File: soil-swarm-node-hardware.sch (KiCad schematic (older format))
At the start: 21 parts, among them J3 Conn_01x07, U1 RFD77101, U4 DS18B20U, U5 SST26VF016B

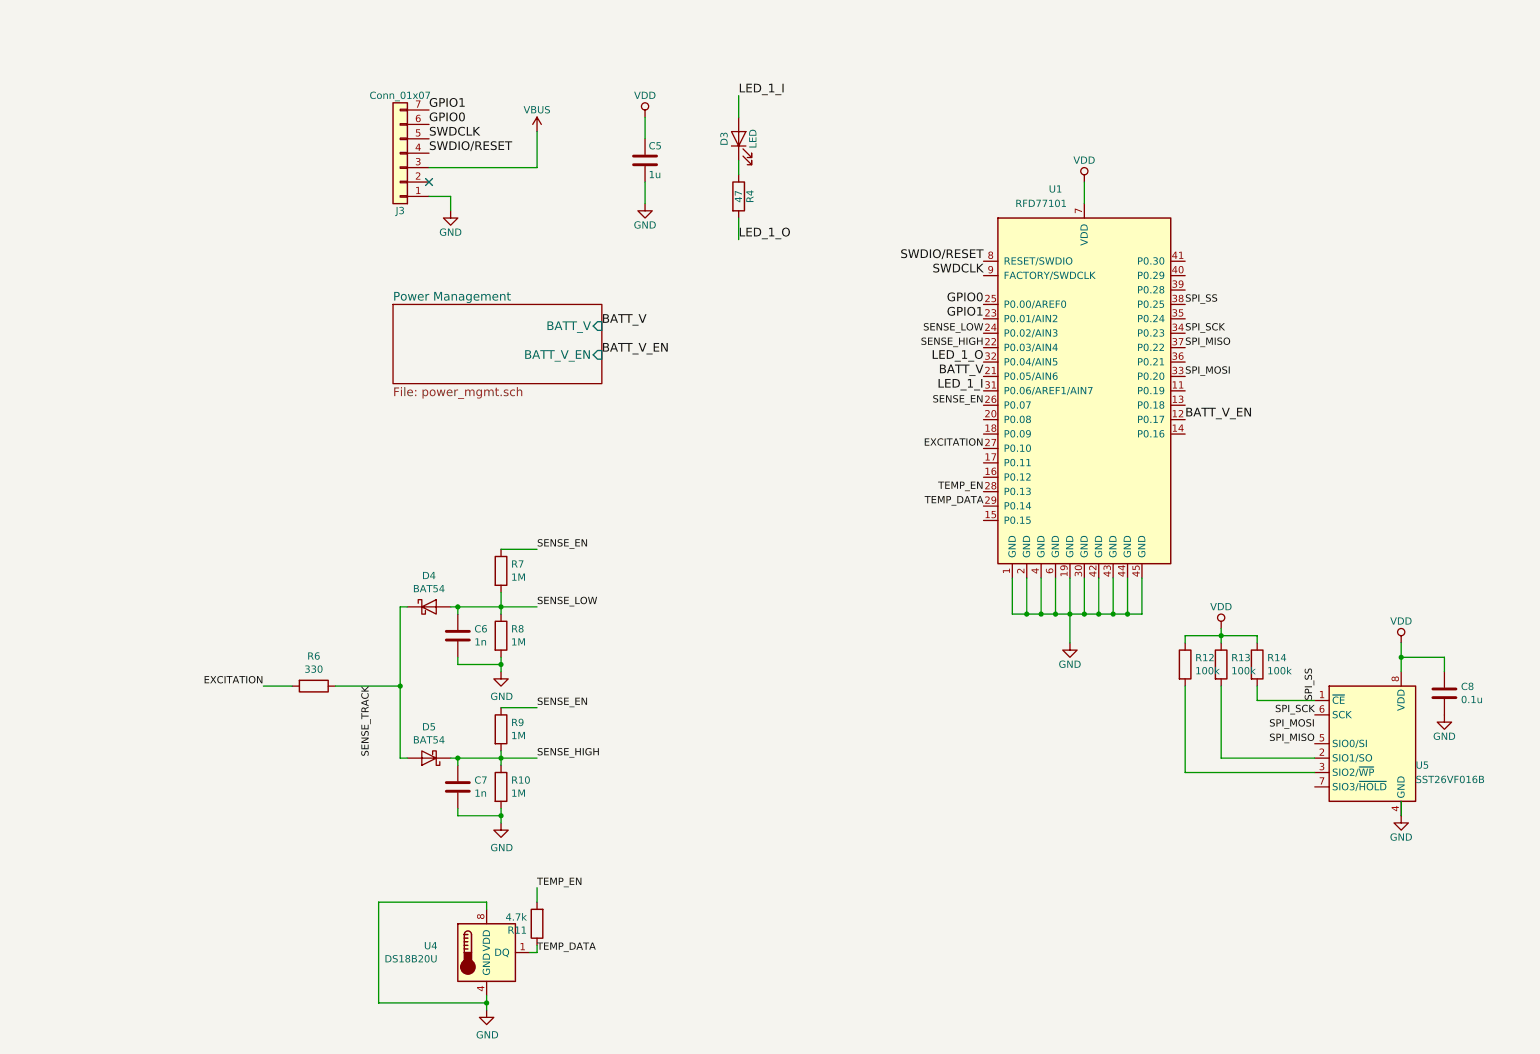
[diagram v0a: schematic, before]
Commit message: create new version based on nRF52840
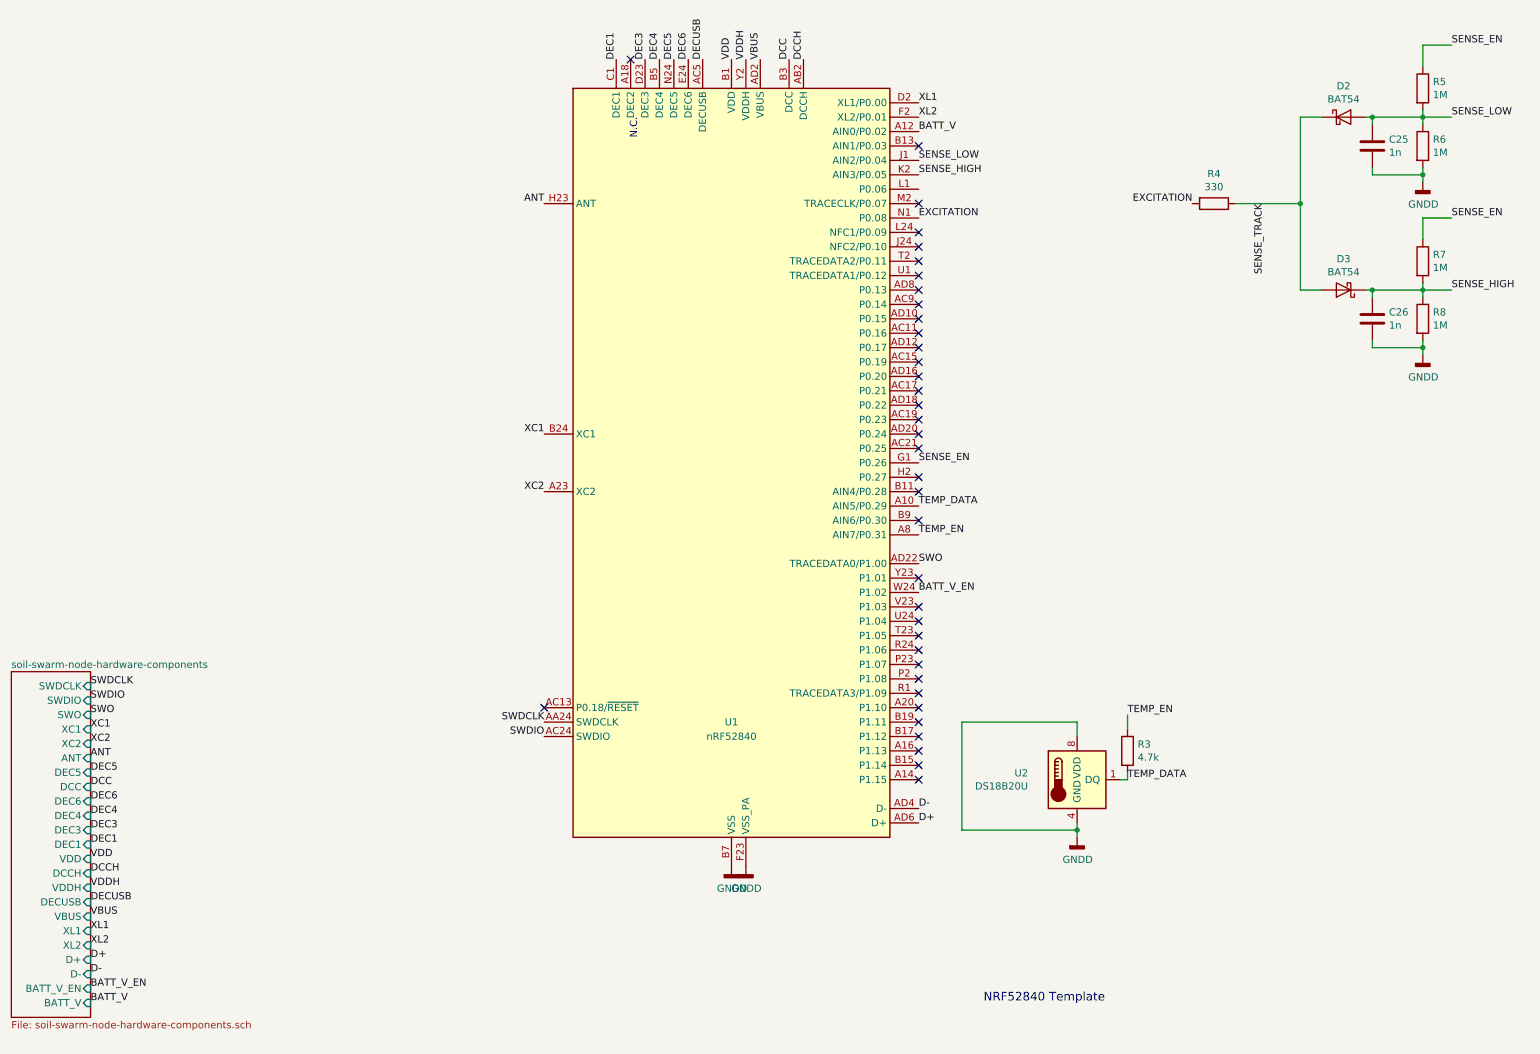
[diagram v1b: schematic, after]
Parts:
- removed C5: 1u, Capacitor_SMD:C_0603_1608Metric, symbol Device:C
- removed C6, C7: 1n, Capacitor_SMD:C_0603_1608Metric, symbol Device:C
- removed C8: 0.1u, Capacitor_SMD:C_0603_1608Metric, symbol Device:C
- removed D3: LED, LED_SMD:LED_0603_1608Metric, symbol Device:LED
- removed D4, D5: BAT54, Diode_SMD:D_SOD-323, symbol Device:D_Schottky
- removed J3: Conn_01x07, Connector_PinHeader_2.54mm:PinHeader_1x07_P2.54mm_Vertical, symbol Connector_Generic:Conn_01x07
- removed R10, R9: 1M, Resistor_SMD:R_0603_1608Metric, symbol Device:R
- removed R11: 4.7k, Resistor_SMD:R_0603_1608Metric, symbol Device:R
- removed R12, R13, R14: 100k, Resistor_SMD:R_0603_1608Metric, symbol Device:R
- removed U1: RFD77101, RF_Module:RFDigital_RFD77101, symbol RF_Bluetooth:RFD77101
- removed U4: DS18B20U, Package_SO:MSOP-8_3x3mm_P0.65mm, symbol Sensor_Temperature:DS18B20U
- removed U5: SST26VF016B, Package_SO:SOIC-8_3.9x4.9mm_P1.27mm, symbol Memory_Flash:SST26VF016B
- added C25, C26: 1n, Capacitor_SMD:C_0402_1005Metric, symbol Device:C
- added D2, D3: BAT54, Diode_SMD:D_SOD-323, symbol Device:D_Schottky
- added R3: 4.7k, Resistor_SMD:R_0402_1005Metric, symbol Device:R
- added R5: 1M, Resistor_SMD:R_0402_1005Metric, symbol Device:R
- added U1: nRF52840, Package_DFN_QFN:Nordic_AQFN-73-1EP_7x7mm_P0.5mm, symbol MCU_Nordic:nRF52840
- added U2: DS18B20U, Package_SO:MSOP-8_3x3mm_P0.65mm, symbol Sensor_Temperature:DS18B20U
- R4: value 47 -> 330; footprint Resistor_SMD:R_0603_1608Metric -> Resistor_SMD:R_0402_1005Metric
- R6: value 330 -> 1M; footprint Resistor_SMD:R_0603_1608Metric -> Resistor_SMD:R_0402_1005Metric
- R7, R8: footprint Resistor_SMD:R_0603_1608Metric -> Resistor_SMD:R_0402_1005Metric
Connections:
- net LED_1_O is gone; now on net EXCITATION: R4.2
- net BATT_V: now also U1.A12 (AIN0/P0.02)
- net BATT_V_EN: now also U1.W24 (P1.02)
- net EXCITATION: now also U1.N1 (P0.08); no longer R6.2
- net SENSE_EN: now also R5.1, U1.G1 (P0.26)
- net SENSE_HIGH: now also R7.2, R8.1, C26.1, D3.1 (K), U1.K2 (AIN3/P0.05)
- net SENSE_LOW: now also R6.1, C25.1, D2.2 (A), R5.2, U1.J1 (AIN2/P0.04); no longer R7.2, R8.1
- net SENSE_TRACK: now also R4.1, D2.1 (K), D3.2 (A); no longer R6.1
- net SWDCLK: now also U1.AA24 (SWDCLK)
- net TEMP_DATA: now also R3.2, U1.A10 (AIN5/P0.29), U2.1 (DQ)
- net TEMP_EN: now also R3.1, U1.A8 (AIN7/P0.31)
- net VBUS: now also U1.AD2 (VBUS)
- net VDD: now also U1.A22 (VDD), U1.AD14 (VDD), U1.AD23 (VDD), U1.B1 (VDD), U1.W1 (VDD)
- net GND renamed GNDD
- net GNDD: now also R6.2, C25.2, C26.2, U1.B7 (VSS), U1.EP (VSS), U1.F23 (VSS_PA), U2.4 (GND), U2.8 (VDD)
- new net ANT: U1.H23 (ANT)
- new net D+: U1.AD6 (D+)
- new net D-: U1.AD4 (D-)
- new net DCC: U1.B3 (DCC)
- new net DCCH: U1.AB2 (DCCH)
- new net DEC1: U1.C1 (DEC1)
- new net DEC3: U1.D23 (DEC3)
- new net DEC4: U1.B5 (DEC4)
- new net DEC5: U1.N24 (DEC5)
- new net DEC6: U1.E24 (DEC6)
- new net DECUSB: U1.AC5 (DECUSB)
- new net SWDIO: U1.AC24 (SWDIO)
- new net SWO: U1.AD22 (TRACEDATA0/P1.00)
- new net VDDH: U1.Y2 (VDDH)
- new net XC1: U1.B24 (XC1)
- new net XC2: U1.A23 (XC2)
- new net XL1: U1.D2 (XL1/P0.00)
- new net XL2: U1.F2 (XL2/P0.01)
- no-connect marks 1 -> 37
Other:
- note added: "N.C."
- note added: "NRF52840 Template"
